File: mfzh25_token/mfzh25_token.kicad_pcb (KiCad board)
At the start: 2 copper layers, 58.1 x 67.9 mm, 39 parts, among them J2 Conn_02x03_Odd_Even

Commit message: almost there
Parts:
- removed the G*** at (72.0, 112.5)
- TP1, TP2, TP3: footprint TestPoint:TestPoint_Pad_D2.0mm -> TestPoint:TestPoint_Pad_D1.5mm
- TP10: value E -> MF RR; footprint TestPoint:TestPoint_Pad_D2.0mm -> TestPoint:TestPoint_Pad_D1.5mm
- TP4: footprint TestPoint:TestPoint_Pad_D1.0mm -> TestPoint:TestPoint_Pad_D1.5mm
- TP6: value A -> AA EI; footprint TestPoint:TestPoint_Pad_D2.0mm -> TestPoint:TestPoint_Pad_D1.5mm
- TP7: value B -> KR RF; footprint TestPoint:TestPoint_Pad_D2.0mm -> TestPoint:TestPoint_Pad_D1.5mm
- TP8: value C -> MI RE; footprint TestPoint:TestPoint_Pad_D2.0mm -> TestPoint:TestPoint_Pad_D1.5mm
- TP9: value D -> AR KF; footprint TestPoint:TestPoint_Pad_D2.0mm -> TestPoint:TestPoint_Pad_D1.5mm
- moved R7 60.7 mm to (94.0, 127.0), turned to -90 degrees
- moved R6 58.1 mm to (88.9, 124.5), turned to -90 degrees
- moved R8 57.3 mm to (94.0, 121.9), turned to -90 degrees
- moved R11 54.2 mm to (78.7, 124.5), turned to 90 degrees
- moved R9 48.7 mm to (83.8, 127.0), turned to -90 degrees
- moved R10 45.5 mm to (83.8, 121.9), turned to -90 degrees
- moved R15 43.1 mm to (73.7, 127.0), turned to 90 degrees
- moved R12 42.7 mm to (68.6, 124.5), turned to 90 degrees
- moved R18 42.6 mm to (63.5, 127.0), turned to 90 degrees
- moved R14 42.4 mm to (73.7, 121.9), turned to 90 degrees
- moved R17 39.2 mm to (58.4, 124.5), turned to 90 degrees
- moved R16 36.6 mm to (48.3, 124.5), turned to 90 degrees
- moved R13 35.1 mm to (63.5, 121.9), turned to 90 degrees
- moved R19 32.7 mm to (53.3, 127.0), turned to 90 degrees
- moved R20 27.7 mm to (53.3, 121.9), turned to 90 degrees
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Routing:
- net Net-(D4-A): track 0.00 -> 41.3 mm, vias 0 -> 2
- net Net-(D3-A): track 0.00 -> 37.9 mm, vias 0 -> 2
- net Net-(R4-Pad2): track 0.00 -> 37.4 mm, vias 0 -> 2
- net Net-(D1-A): track 0.00 -> 33.3 mm, vias 0 -> 2
- net Net-(R3-Pad2): track 0.00 -> 30.0 mm, vias 0 -> 2
- net Net-(D2-A): track 0.00 -> 29.9 mm, vias 0 -> 2
- net Net-(R10-Pad1): track 0.00 -> 27.9 mm, vias 0 -> 2
- net Net-(R2-Pad2): track 0.00 -> 27.3 mm, vias 0 -> 2
- net Net-(D5-A): track 0.00 -> 26.9 mm, vias 0 -> 2
- net Net-(R1-Pad2): track 0.00 -> 26.3 mm, vias 0 -> 2
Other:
- board text added: "(Crypto as in Cryptography, not bitcoin D: )"
- board text added: "Crypto Challenge By ElectroNick"

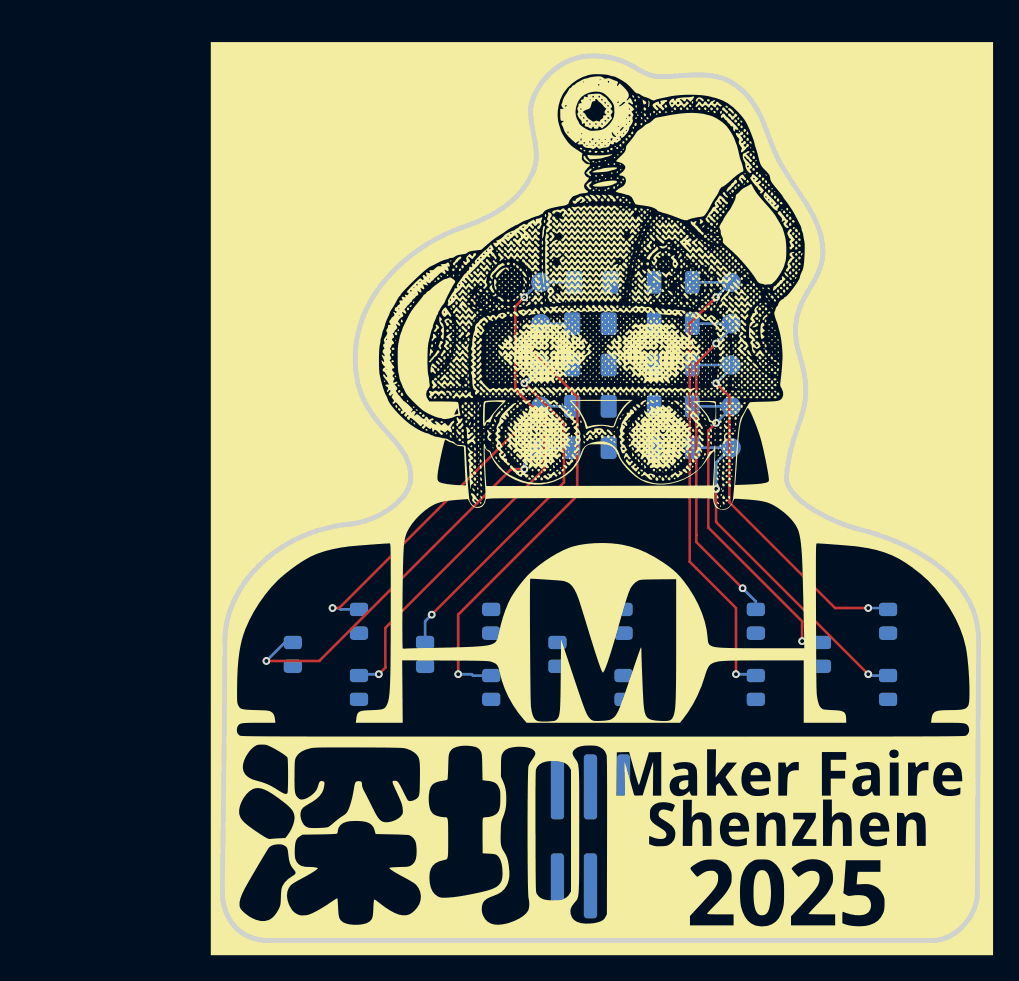
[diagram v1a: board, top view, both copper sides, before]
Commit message: pcb done, send to fabrication
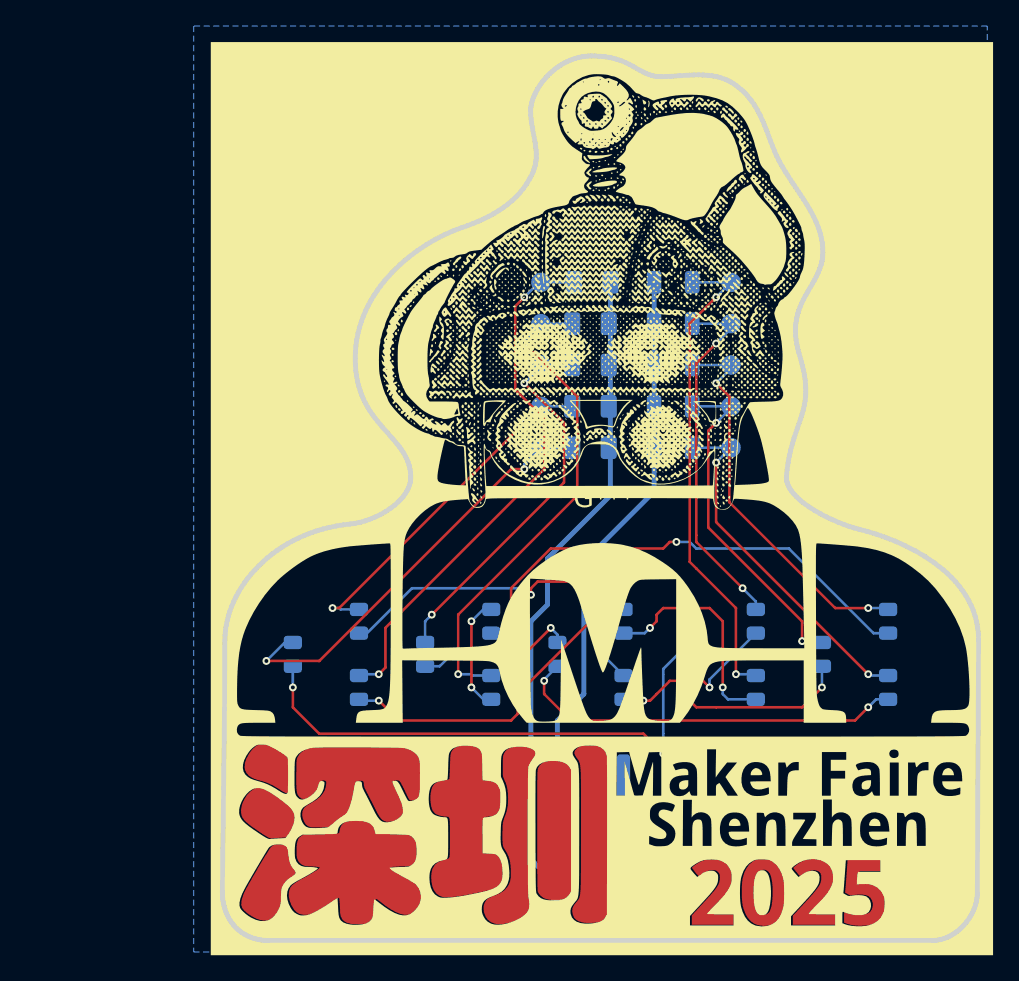
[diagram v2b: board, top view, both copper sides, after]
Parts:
- added G***: LOGO, LOGO, F.Cu at (72.1, 112.5)
- added G***: LOGO, LOGO, B.Cu at (76.7, 138.7)
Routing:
- net GND: track 0.00 -> 49.7 mm
- net Net-(R11-Pad2): track 0.00 -> 42.4 mm, vias 0 -> 2
- net VCC: track 0.00 -> 41.8 mm
- net Net-(R13-Pad1): track 0.00 -> 38.5 mm, vias 0 -> 2
- net Net-(R12-Pad1): track 0.00 -> 30.5 mm, vias 0 -> 2
- net Net-(R15-Pad2): track 0.00 -> 28.6 mm, vias 0 -> 2
- net Net-(R14-Pad2): track 0.00 -> 25.5 mm, vias 0 -> 2
- net Net-(R14-Pad1): track 0.00 -> 17.4 mm, vias 0 -> 2
- net Net-(R11-Pad1): track 0.00 -> 15.3 mm, vias 0 -> 2
- net Net-(R10-Pad2): track 0.00 -> 13.1 mm, vias 0 -> 2
- net Net-(R12-Pad2): track 0.00 -> 12.2 mm, vias 0 -> 2
- net Net-(R13-Pad2): track 0.00 -> 8.88 mm, vias 0 -> 2
- added copper zone on B.Cu, net GND
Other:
- board text added: "Solder Challenge"
- board text added: "The key of being a maker is learning new skills, learning new languages, overcome challenges, making commuinity, new friends. What's your key?"
- board text added: "Xtqijw Hmfqqjslj RfpjwKfnwj Xmjsemjs 2025"
- board text added: "myyux://jqjhywtsnhp-ht.lnymzg.nt/rkex25/"
- board text added: "| M A K E R --|--------------- F | R G E N H --|--------------- A | L C B P X --|--------------- I | A Z U A Y --|--------------- R | R R C D O --|--------------- E | W R Q S R"
